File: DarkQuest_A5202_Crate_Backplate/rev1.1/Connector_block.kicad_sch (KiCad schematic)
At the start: 27 parts, among them J1 Conn_01x02_Pin, J2 HSEC8-170-01-X-DV-A, U1 MCP23017_SS

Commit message: Add cmos switches with squashed commits
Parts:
- removed C1, C2: 0.1 µF, Capacitor_SMD:C_0201_0603Metric, symbol PCM_SL_Devices:Capacitor_NP
- removed R1, R2: 4.7k or 2.2k, Resistor_SMD:R_0201_0603Metric, symbol Device:R
- removed R3: 10k, Resistor_SMD:R_0201_0603Metric, symbol Device:R
- removed R4, R5: 100, Resistor_SMD:R_0201_0603Metric, symbol Device:R
- removed U1: MCP23017_SS, Package_SO:SSOP-28_5.3x10.2mm_P0.65mm, symbol Interface_Expansion:MCP23017_SS
- C1: renamed from C3; footprint Capacitor_SMD:C_0201_0603Metric -> Capacitor_SMD:C_0402_1005Metric
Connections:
- no-connect marks 2 -> 3

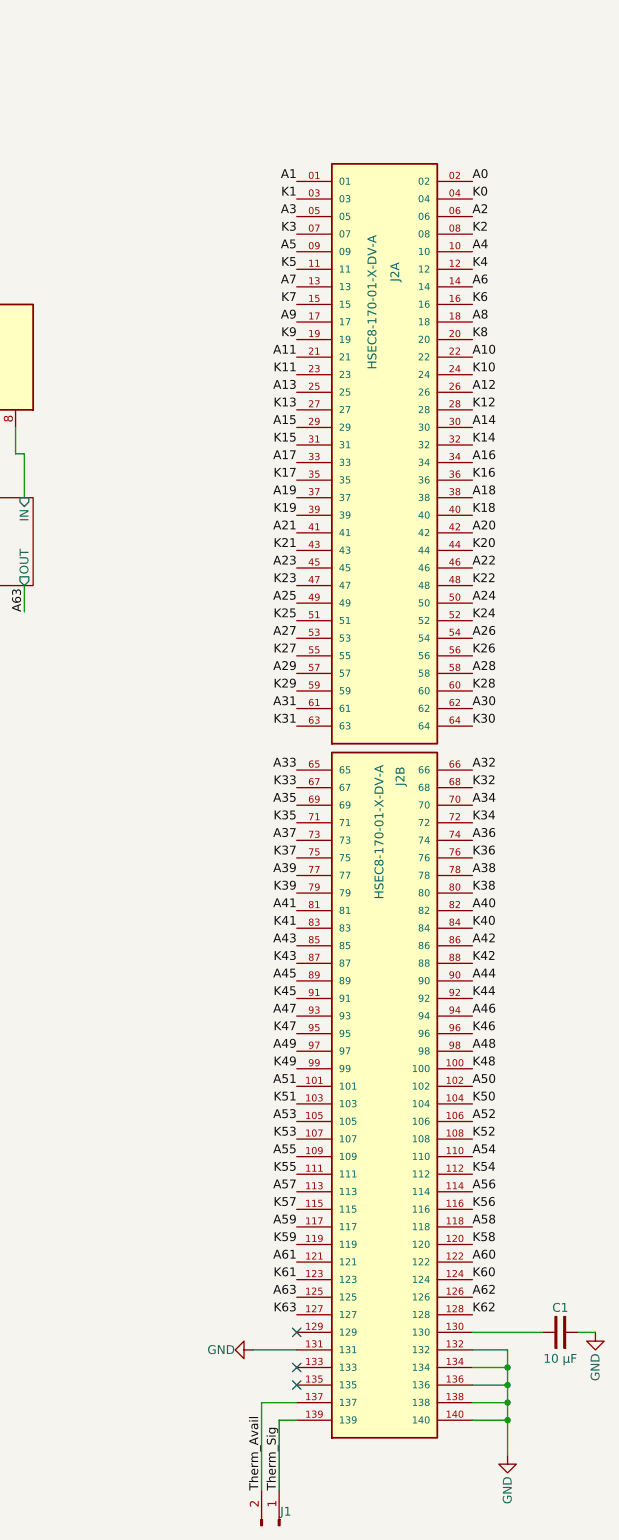
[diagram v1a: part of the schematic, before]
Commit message: Modify A5202 pinout numbering, clean silk and fab layers
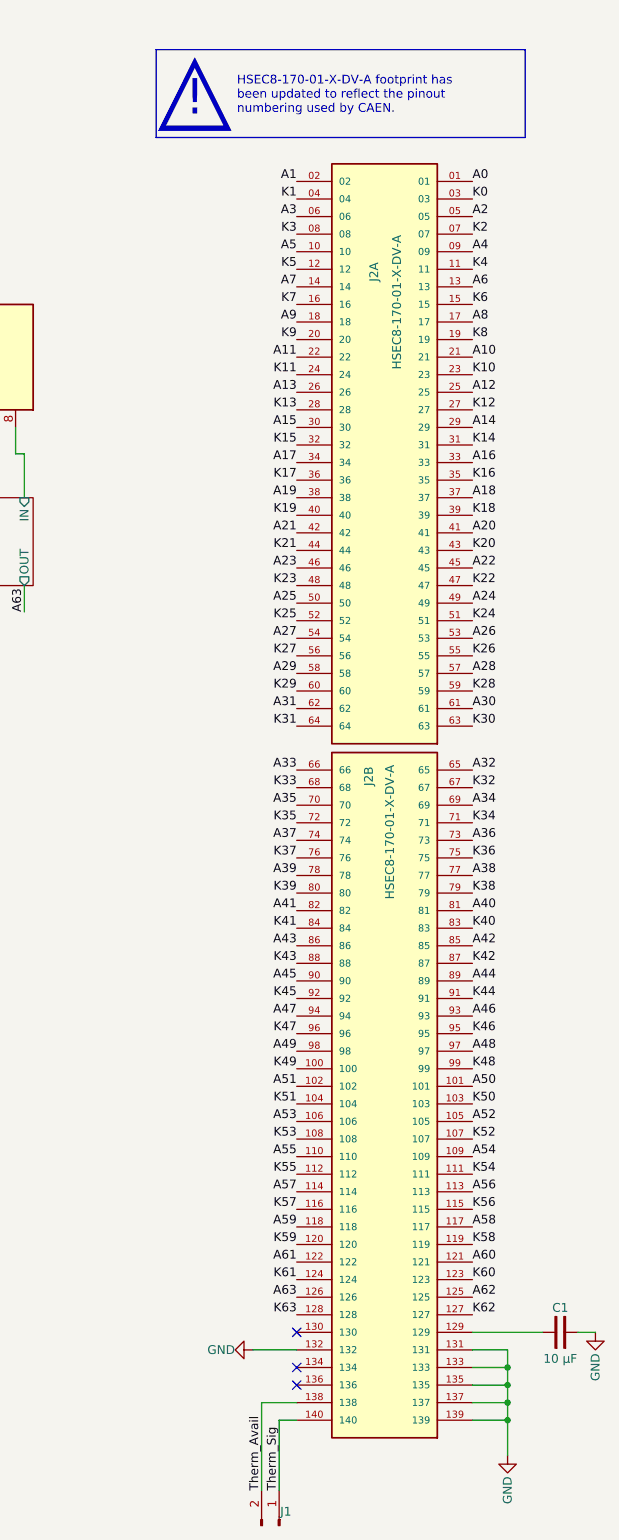
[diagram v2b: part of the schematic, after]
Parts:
- J2: footprint HSEC8_170_01_S_DV_A_K:SAMTEC_HSEC8-170-01-X-DV-A -> A5202_Backplate:SAMTEC_HSEC8-170-01-X-DV-A-CAEN-PINOUT
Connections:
- net A0: now also J2.01; no longer J2.02
- net A1: now also J2.02; no longer J2.01
- net A10: now also J2.21; no longer J2.22
- net A11: now also J2.22; no longer J2.21
- net A12: now also J2.25; no longer J2.26
- net A13: now also J2.26; no longer J2.25
- net A14: now also J2.29; no longer J2.30
- net A15: now also J2.30; no longer J2.29
- net A16: now also J2.33; no longer J2.34
- net A17: now also J2.34; no longer J2.33
- net A18: now also J2.37; no longer J2.38
- net A19: now also J2.38; no longer J2.37
- net A2: now also J2.05; no longer J2.06
- net A20: now also J2.41; no longer J2.42
- net A21: now also J2.42; no longer J2.41
- net A22: now also J2.45; no longer J2.46
- net A23: now also J2.46; no longer J2.45
- net A24: now also J2.49; no longer J2.50
- net A25: now also J2.50; no longer J2.49
- net A26: now also J2.53; no longer J2.54
- net A27: now also J2.54; no longer J2.53
- net A28: now also J2.57; no longer J2.58
- net A29: now also J2.58; no longer J2.57
- net A3: now also J2.06; no longer J2.05
- net A30: now also J2.61; no longer J2.62
- net A31: now also J2.62; no longer J2.61
- net A32: now also J2.65; no longer J2.66
- net A33: now also J2.66; no longer J2.65
- net A34: now also J2.69; no longer J2.70
- net A35: now also J2.70; no longer J2.69
- net A36: now also J2.73; no longer J2.74
- net A37: now also J2.74; no longer J2.73
- net A38: now also J2.77; no longer J2.78
- net A39: now also J2.78; no longer J2.77
- net A4: now also J2.09; no longer J2.10
- net A40: now also J2.81; no longer J2.82
- net A41: now also J2.82; no longer J2.81
- net A42: now also J2.85; no longer J2.86
- net A43: now also J2.86; no longer J2.85
- net A44: now also J2.89; no longer J2.90
- net A45: now also J2.90; no longer J2.89
- net A46: now also J2.93; no longer J2.94
- net A47: now also J2.94; no longer J2.93
- net A48: now also J2.97; no longer J2.98
- net A49: now also J2.98; no longer J2.97
- net A5: now also J2.10; no longer J2.09
- net A50: now also J2.101; no longer J2.102
- net A51: now also J2.102; no longer J2.101
- net A52: now also J2.105; no longer J2.106
- net A53: now also J2.106; no longer J2.105
- net A54: now also J2.109; no longer J2.110
- net A55: now also J2.110; no longer J2.109
- net A56: now also J2.113; no longer J2.114
- net A57: now also J2.114; no longer J2.113
- net A58: now also J2.117; no longer J2.118
- net A59: now also J2.118; no longer J2.117
- net A6: now also J2.13; no longer J2.14
- net A60: now also J2.121; no longer J2.122
- net A61: now also J2.122; no longer J2.121
- net A62: now also J2.125; no longer J2.126
- net A63: now also J2.126; no longer J2.125
- net A7: now also J2.14; no longer J2.13
- net A8: now also J2.17; no longer J2.18
- net A9: now also J2.18; no longer J2.17
- net GND: now also J2.133, J2.135, J2.137, J2.139; no longer J2.134, J2.136, J2.138, J2.140
- net K0: now also J2.03; no longer J2.04
- net K1: now also J2.04; no longer J2.03
- net K10: now also J2.23; no longer J2.24
- net K11: now also J2.24; no longer J2.23
- net K12: now also J2.27; no longer J2.28
- net K13: now also J2.28; no longer J2.27
- net K14: now also J2.31; no longer J2.32
- net K15: now also J2.32; no longer J2.31
- net K16: now also J2.35; no longer J2.36
- net K17: now also J2.36; no longer J2.35
- net K18: now also J2.39; no longer J2.40
- net K19: now also J2.40; no longer J2.39
- net K2: now also J2.07; no longer J2.08
- net K20: now also J2.43; no longer J2.44
- net K21: now also J2.44; no longer J2.43
- net K22: now also J2.47; no longer J2.48
- net K23: now also J2.48; no longer J2.47
- net K24: now also J2.51; no longer J2.52
- net K25: now also J2.52; no longer J2.51
- net K26: now also J2.55; no longer J2.56
- net K27: now also J2.56; no longer J2.55
- net K28: now also J2.59; no longer J2.60
- net K29: now also J2.60; no longer J2.59
- net K3: now also J2.08; no longer J2.07
- net K30: now also J2.63; no longer J2.64
- net K31: now also J2.64; no longer J2.63
- net K32: now also J2.67; no longer J2.68
- net K33: now also J2.68; no longer J2.67
- net K34: now also J2.71; no longer J2.72
- net K35: now also J2.72; no longer J2.71
- net K36: now also J2.75; no longer J2.76
- net K37: now also J2.76; no longer J2.75
- net K38: now also J2.79; no longer J2.80
- net K39: now also J2.80; no longer J2.79
- net K4: now also J2.11; no longer J2.12
- net K40: now also J2.83; no longer J2.84
- net K41: now also J2.84; no longer J2.83
- net K42: now also J2.87; no longer J2.88
- net K43: now also J2.88; no longer J2.87
- net K44: now also J2.91; no longer J2.92
- net K45: now also J2.92; no longer J2.91
- net K46: now also J2.95; no longer J2.96
- net K47: now also J2.96; no longer J2.95
- net K48: now also J2.99; no longer J2.100
- net K49: now also J2.100; no longer J2.99
- net K5: now also J2.12; no longer J2.11
- net K50: now also J2.103; no longer J2.104
- net K51: now also J2.104; no longer J2.103
- net K52: now also J2.107; no longer J2.108
- net K53: now also J2.108; no longer J2.107
- net K54: now also J2.111; no longer J2.112
- net K55: now also J2.112; no longer J2.111
- net K56: now also J2.115; no longer J2.116
- net K57: now also J2.116; no longer J2.115
- net K58: now also J2.119; no longer J2.120
- net K59: now also J2.120; no longer J2.119
- net K6: now also J2.15; no longer J2.16
- net K60: now also J2.123; no longer J2.124
- net K61: now also J2.124; no longer J2.123
- net K62: now also J2.127; no longer J2.128
- net K63: now also J2.128; no longer J2.127
- net K7: now also J2.16; no longer J2.15
- net K8: now also J2.19; no longer J2.20
- net K9: now also J2.20; no longer J2.19
- net Therm_Avail: now also J2.138; no longer J2.137
- net Therm_Sig: now also J2.140; no longer J2.139
- net at C1.2: now also J2.129; no longer J2.130
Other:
- note added: "!"
- note added: "HSEC8-170-01-X-DV-A footprint has been updated to reflect the pinout numbering used by CAEN."
- note added: "△"
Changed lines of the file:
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@@
 		(comment 1 "Nathan Raplee")
 	)
+	(rectangle
+		(start 482.6 20.32)
+		(end 535.94 33.02)
+		(stroke
+			(width 0)
+			(type default)
+			(color 221 133 0 1)
+		)
+		(fill
+			(type none)
+		)
+	)
+	(text "!"
+		(exclude_from_sim no)
+		(at 488.188 27.432 0)
+		(effects
+			(font
+				(size 5.08 5.08)
+				(color 221 133 0 1)
+			)
+		)
+	)
+	(text "HSEC8-170-01-X-DV-A footprint has \nbeen updated to reflect the pinout \nnumbering used by CAEN."
+		(exclude_from_sim no)
+		(at 494.284 26.924 0)
+		(effects
+			(font
+				(size 1.27 1.27)
+				(color 221 133 0 1)
+			)
+			(justify left)
+		)
+	)
+	(text "△"
+		(exclude_from_sim no)
+		(at 488.188 25.908 0)
+		(effects
+			(font
+				(size 10.16 10.16)
+				(color 221 133 0 1)
+			)
+		)
+	)
 	(junction
 		(at 199.39 49.53)
@@
 		(lib_id "HSEC8-170-01-X-DV-A:HSEC8-170-01-X-DV-A")
 		(at 515.62 170.18 0)
+		(mirror y)
 		(unit 2)
 		(exclude_from_sim no)
@@
 		(dnp no)
 		(property "Reference" "J2"
-			(at 517.906 123.952 90)
+			(at 513.334 123.952 90)
 			(effects
 				(font
@@
 		)
 		(property "Value" "HSEC8-170-01-X-DV-A"
-			(at 514.858 123.698 90)
+			(at 516.382 123.698 90)
 			(effects
 				(font
@@
 			)
 		)
-		(property "Footprint" "HSEC8_170_01_S_DV_A_K:SAMTEC_HSEC8-170-01-X-DV-A"
+		(property "Footprint" "A5202_Backplate:SAMTEC_HSEC8-170-01-X-DV-A-CAEN-PINOUT"
 			(at 515.62 170.18 0)
 			(effects
@@
 		(lib_id "HSEC8-170-01-X-DV-A:HSEC8-170-01-X-DV-A")
 		(at 515.62 77.47 0)
+		(mirror y)
 		(unit 1)
 		(exclude_from_sim no)
@@
 		(dnp no)
 		(property "Reference" "J2"
-			(at 517.144 51.054 90)
+			(at 514.096 51.054 90)
 			(effects
 				(font
@@
 		)
 		(property "Value" "HSEC8-170-01-X-DV-A"
-			(at 513.842 66.548 90)
+			(at 517.398 66.548 90)
 			(effects
 				(font
@@
 			)
 		)
-		(property "Footprint" "HSEC8_170_01_S_DV_A_K:SAMTEC_HSEC8-170-01-X-DV-A"
+		(property "Footprint" "A5202_Backplate:SAMTEC_HSEC8-170-01-X-DV-A-CAEN-PINOUT"
 			(at 515.62 77.47 0)
 			(effects
